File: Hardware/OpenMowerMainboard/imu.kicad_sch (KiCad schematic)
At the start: 1 part, among them J20 Conn_01x10_Female

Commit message: chore: remove space before PN
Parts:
- J20: Part Number PZ254-1-10-Z-8.5 -> PZ254-1-10-Z-8.5
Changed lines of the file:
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@@
       (effects (font (size 1.27 1.27)) hide)
     )
-    (property "Part Number" "	PZ254-1-10-Z-8.5" (id 5) (at 162.56 66.04 0)
+    (property "Part Number" "PZ254-1-10-Z-8.5" (id 5) (at 162.56 66.04 0)
       (effects (font (size 1.27 1.27)) hide)
     )

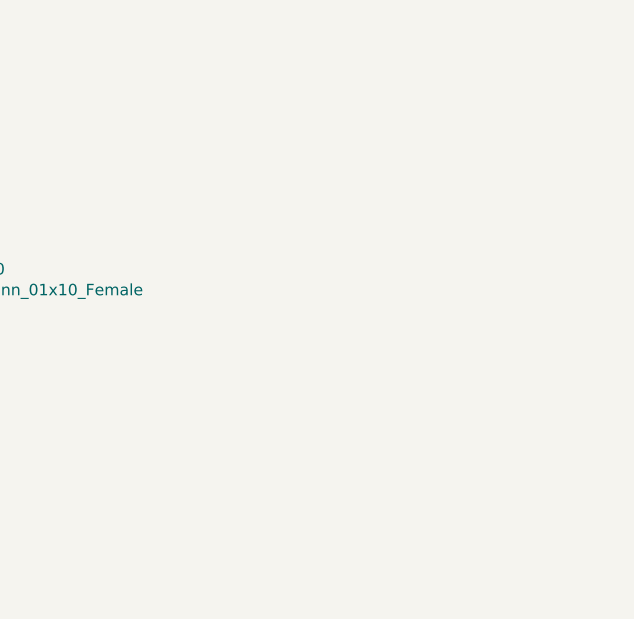
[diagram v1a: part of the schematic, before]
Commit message: feat(imu): additional pin header for WT901
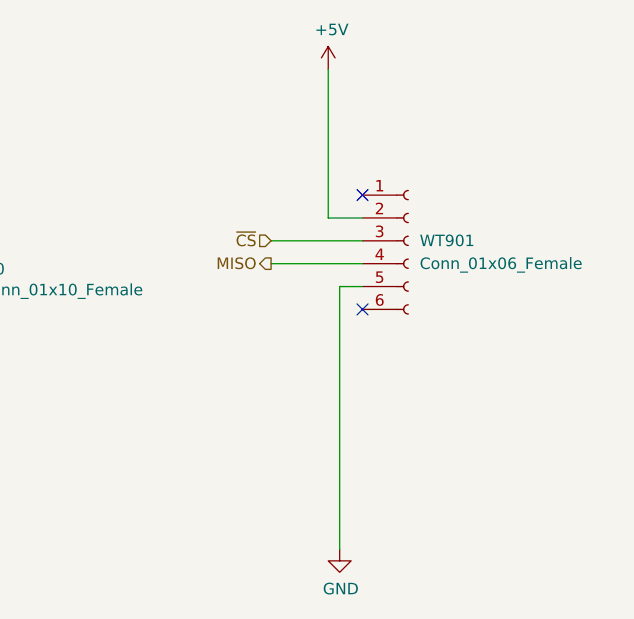
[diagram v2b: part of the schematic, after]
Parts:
- added WT901: Conn_01x06_Female, MyModules:WT901, symbol Connector:Conn_01x06_Female
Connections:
- net +5V: now also WT901.2 (Pin_2)
- net GND: now also WT901.5 (Pin_5)
- net MISO: now also WT901.4 (Pin_4)
- net ~{CS}: now also WT901.3 (Pin_3)
- no-connect marks 4 -> 6
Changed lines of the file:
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@@
   (no_connect (at 157.48 68.58))
   (no_connect (at 157.48 73.66))
+  (no_connect (at 205.74 58.42))
+  (no_connect (at 205.74 71.12))
   (wire (pts (xy 129.54 71.12) (xy 157.48 71.12))
     (stroke (width 0) (type default) (color 0 0 0 0))
@@
     (stroke (width 0) (type default) (color 0 0 0 0))
   )
+  (wire (pts (xy 205.74 68.58) (xy 203.2 68.58))
+    (stroke (width 0) (type default) (color 0 0 0 0))
+  )
+  (wire (pts (xy 205.74 60.96) (xy 201.93 60.96))
+    (stroke (width 0) (type default) (color 0 0 0 0))
+  )
+  (wire (pts (xy 195.58 63.5) (xy 205.74 63.5))
+    (stroke (width 0) (type default) (color 0 0 0 0))
+  )
   (wire (pts (xy 157.48 58.42) (xy 151.13 58.42))
     (stroke (width 0) (type default) (color 0 0 0 0))
   )
+  (wire (pts (xy 203.2 68.58) (xy 203.2 97.79))
+    (stroke (width 0) (type default) (color 0 0 0 0))
+  )
   (wire (pts (xy 129.54 76.2) (xy 157.48 76.2))
+    (stroke (width 0) (type default) (color 0 0 0 0))
+  )
+  (wire (pts (xy 195.58 66.04) (xy 205.74 66.04))
     (stroke (width 0) (type default) (color 0 0 0 0))
   )
@@
     (stroke (width 0) (type default) (color 0 0 0 0))
   )
+  (wire (pts (xy 201.93 60.96) (xy 201.93 44.45))
+    (stroke (width 0) (type default) (color 0 0 0 0))
+  )
   (hierarchical_label "~{CS}" (shape input) (at 129.54 76.2 180)
     (effects (font (size 1.27 1.27)) (justify right))
@@
     (effects (font (size 1.27 1.27)) (justify right))
   )
+  (hierarchical_label "MISO" (shape output) (at 195.58 66.04 180)
+    (effects (font (size 1.27 1.27)) (justify right))
+  )
   (hierarchical_label "SCK" (shape input) (at 129.54 60.96 180)
+    (effects (font (size 1.27 1.27)) (justify right))
+  )
+  (hierarchical_label "~{CS}" (shape input) (at 195.58 63.5 180)
     (effects (font (size 1.27 1.27)) (justify right))
   )
@@
     (pin "1")
   )
+  (symbol (lib_id "power:GND") (at 203.2 97.79 0) (unit 1)
+    (in_bom yes) (on_board yes)
+    (property "Reference" "#PWR0107" (id 0) (at 203.2 104.14 0)
+      (effects (font (size 1.27 1.27)) hide)
+    )
+    (property "Value" "GND" (id 1) (at 203.327 102.1842 0))
+    (property "Footprint" "" (id 2) (at 203.2 97.79 0)
+      (effects (font (size 1.27 1.27)) hide)
+    )
+    (property "Datasheet" "" (id 3) (at 203.2 97.79 0)
+      (effects (font (size 1.27 1.27)) hide)
+    )
+    (pin "1")
+  )
+  (symbol (lib_id "power:+5V") (at 201.93 44.45 0) (unit 1)
+    (in_bom yes) (on_board yes)
+    (property "Reference" "#PWR0106" (id 0) (at 201.93 48.26 0)
+      (effects (font (size 1.27 1.27)) hide)
+    )
+    (property "Value" "+5V" (id 1) (at 202.311 40.0558 0))
+    (property "Footprint" "" (id 2) (at 201.93 44.45 0)
+      (effects (font (size 1.27 1.27)) hide)
+    )
+    (property "Datasheet" "" (id 3) (at 201.93 44.45 0)
+      (effects (font (size 1.27 1.27)) hide)
+    )
+    (pin "1")
+  )
+  (symbol (lib_id "Connector:Conn_01x06_Female") (at 210.82 63.5 0) (unit 1)
+    (in_bom yes) (on_board yes) (fields_autoplaced)
+    (property "Reference" "WT901" (id 0) (at 212.09 63.4999 0)
+      (effects (font (size 1.27 1.27)) (justify left))
+    )
+    (property "Value" "Conn_01x06_Female" (id 1) (at 212.09 66.0399 0)
+      (effects (font (size 1.27 1.27)) (justify left))
+    )
+    (property "Footprint" "MyModules:WT901" (id 2) (at 210.82 63.5 0)
+      (effects (font (size 1.27 1.27)) hide)
+    )
+    (property "Datasheet" "~" (id 3) (at 210.82 63.5 0)
+      (effects (font (size 1.27 1.27)) hide)
+    )
+    (pin "1")
+    (pin "2")
+    (pin "3")
+    (pin "4")
+    (pin "5")
+    (pin "6")
+  )
 )

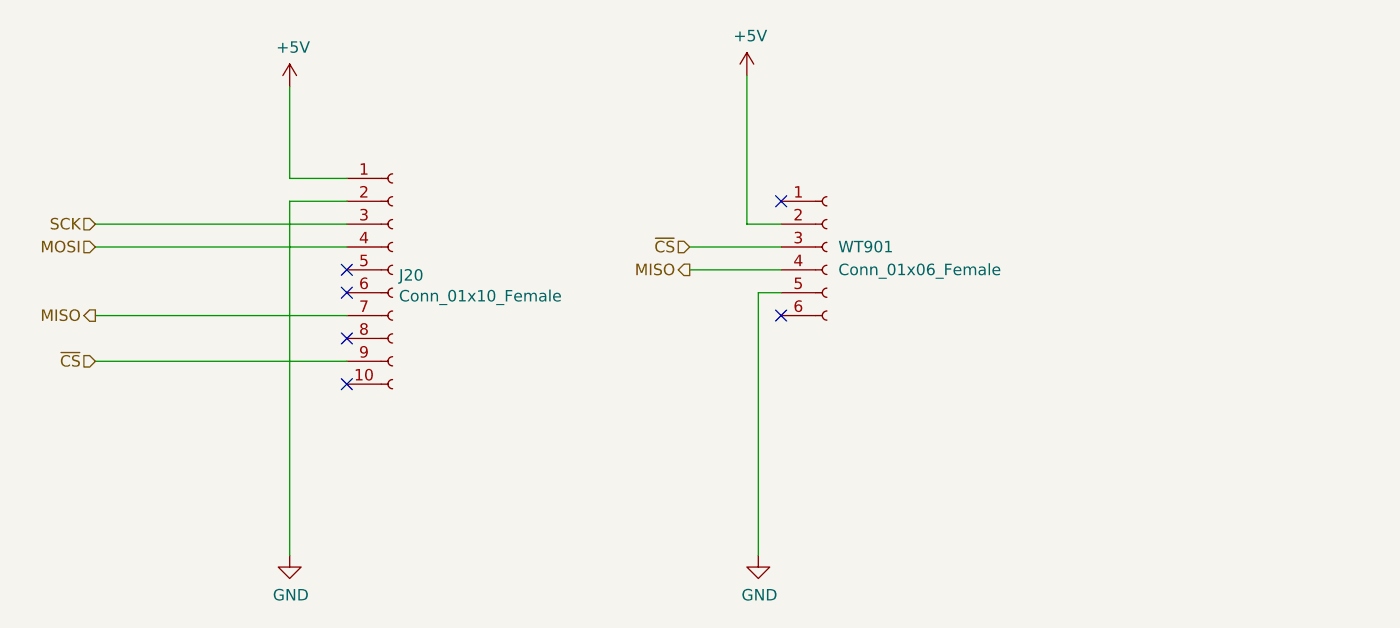
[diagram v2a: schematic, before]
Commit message: fix(imu): update and reroute sound/imu connections
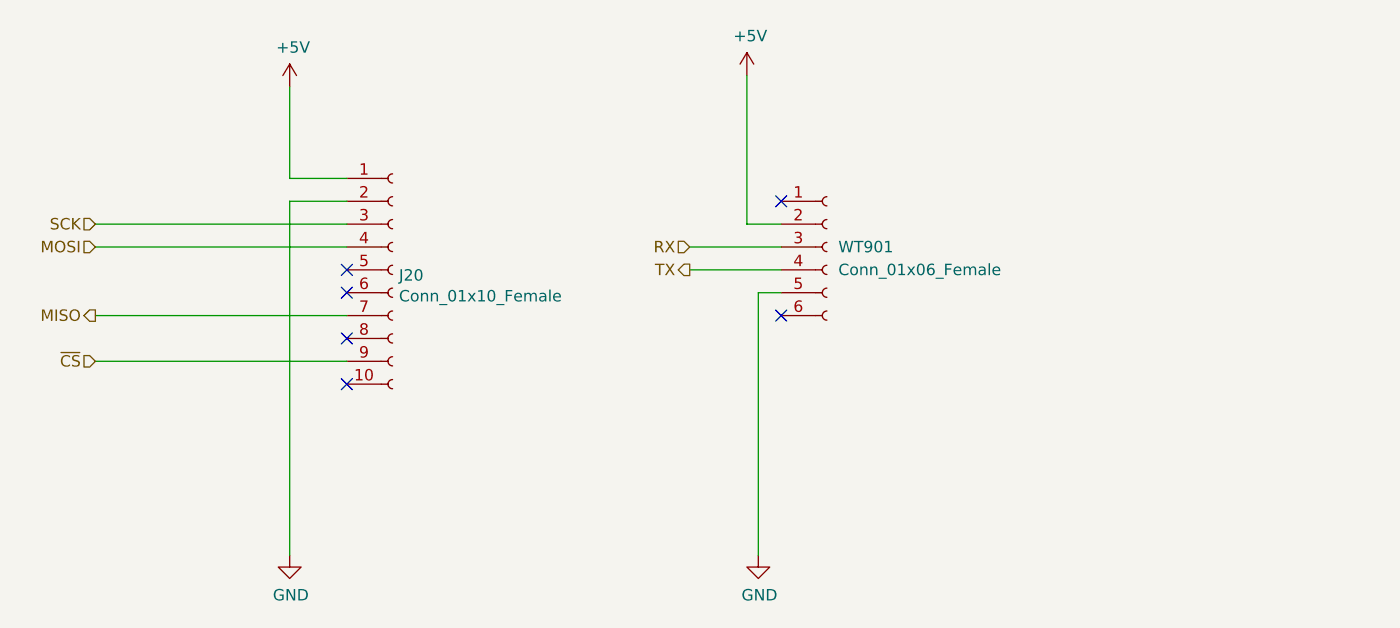
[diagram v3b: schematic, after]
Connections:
- net MISO: no longer WT901.4 (Pin_4)
- net ~{CS}: no longer WT901.3 (Pin_3)
- new net RX: WT901.3 (Pin_3)
- new net TX: WT901.4 (Pin_4)
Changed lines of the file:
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@@
     (effects (font (size 1.27 1.27)) (justify right))
   )
-  (hierarchical_label "MISO" (shape output) (at 195.58 66.04 180)
+  (hierarchical_label "TX" (shape output) (at 195.58 66.04 180)
     (effects (font (size 1.27 1.27)) (justify right))
   )
@@
     (effects (font (size 1.27 1.27)) (justify right))
   )
-  (hierarchical_label "~{CS}" (shape input) (at 195.58 63.5 180)
+  (hierarchical_label "RX" (shape input) (at 195.58 63.5 180)
     (effects (font (size 1.27 1.27)) (justify right))
   )

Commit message: feat(imu): ttl/i2c selector for WT901
+ moved voltage selector for sound
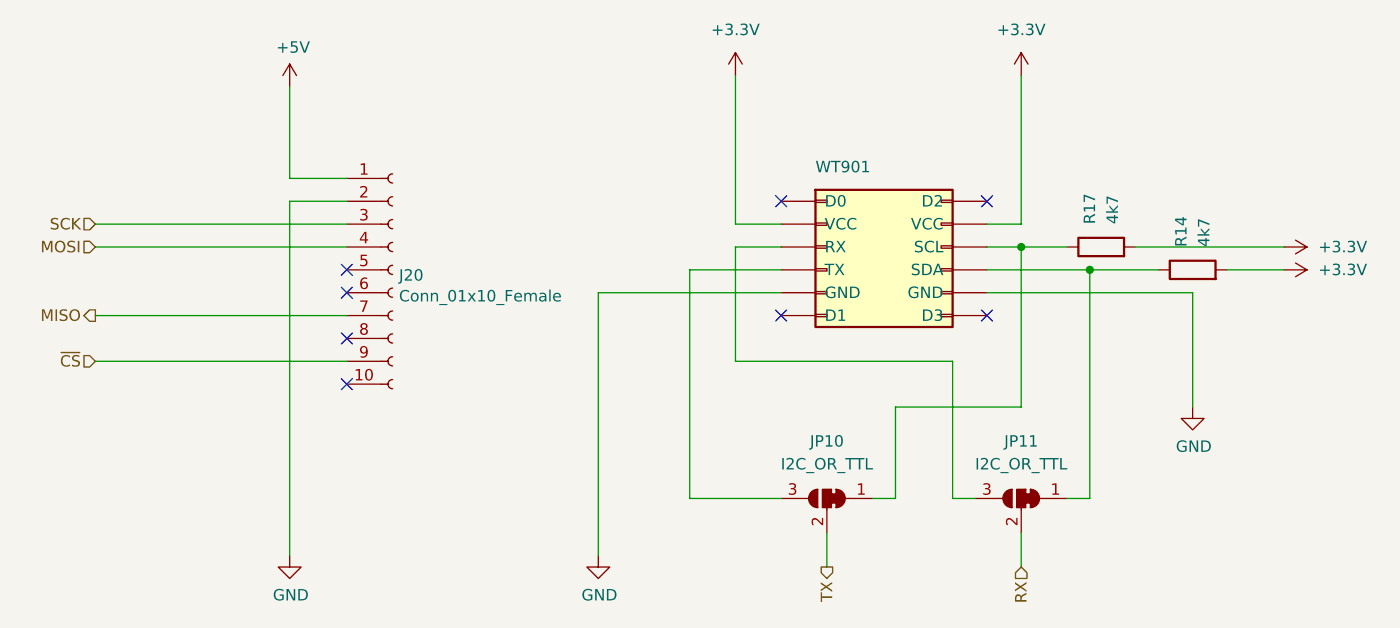
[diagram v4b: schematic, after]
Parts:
- added JP10, JP11: I2C_OR_TTL, Jumper:SolderJumper-3_P1.3mm_Bridged12_Pad1.0x1.5mm, symbol Jumper:SolderJumper_3_Bridged12
- added R14, R17: 4k7, Resistor_SMD:R_0805_2012Metric_Pad1.20x1.40mm_HandSolder, symbol Device:R
- WT901: value Conn_01x06_Female -> Conn_02x06_Female; symbol Connector:Conn_01x06_Female -> Connector_Generic:Conn_02x06_Row_Letter_First
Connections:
- net +5V: no longer WT901.2 (Pin_2)
- net GND: now also WT901.a5 (GND), WT901.b5 (GND); no longer WT901.5 (Pin_5)
- net RX: now also JP11.2 (C); no longer WT901.3 (Pin_3)
- net TX: now also JP10.2 (C); no longer WT901.4 (Pin_4)
- new net: JP11.1 (A), R14.1, WT901.b4 (SDA)
- new net: JP11.3 (B), WT901.a3 (RX)
- new net: JP10.1 (A), R17.1, WT901.b3 (SCL)
- new net: JP10.3 (B), WT901.a4 (TX)
- new net +3V3: R14.2, R17.2, WT901.a2 (VCC), WT901.b2 (VCC)
- no-connect marks 6 -> 8
